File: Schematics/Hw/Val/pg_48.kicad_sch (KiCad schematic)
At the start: 20 parts, among them U5001 F30, U5002 F151, U5003 F37, U5004 F37, U5005 F04, U5006 F02, U5007 F00, U5008 F37, U5009 F37, U5010 F04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

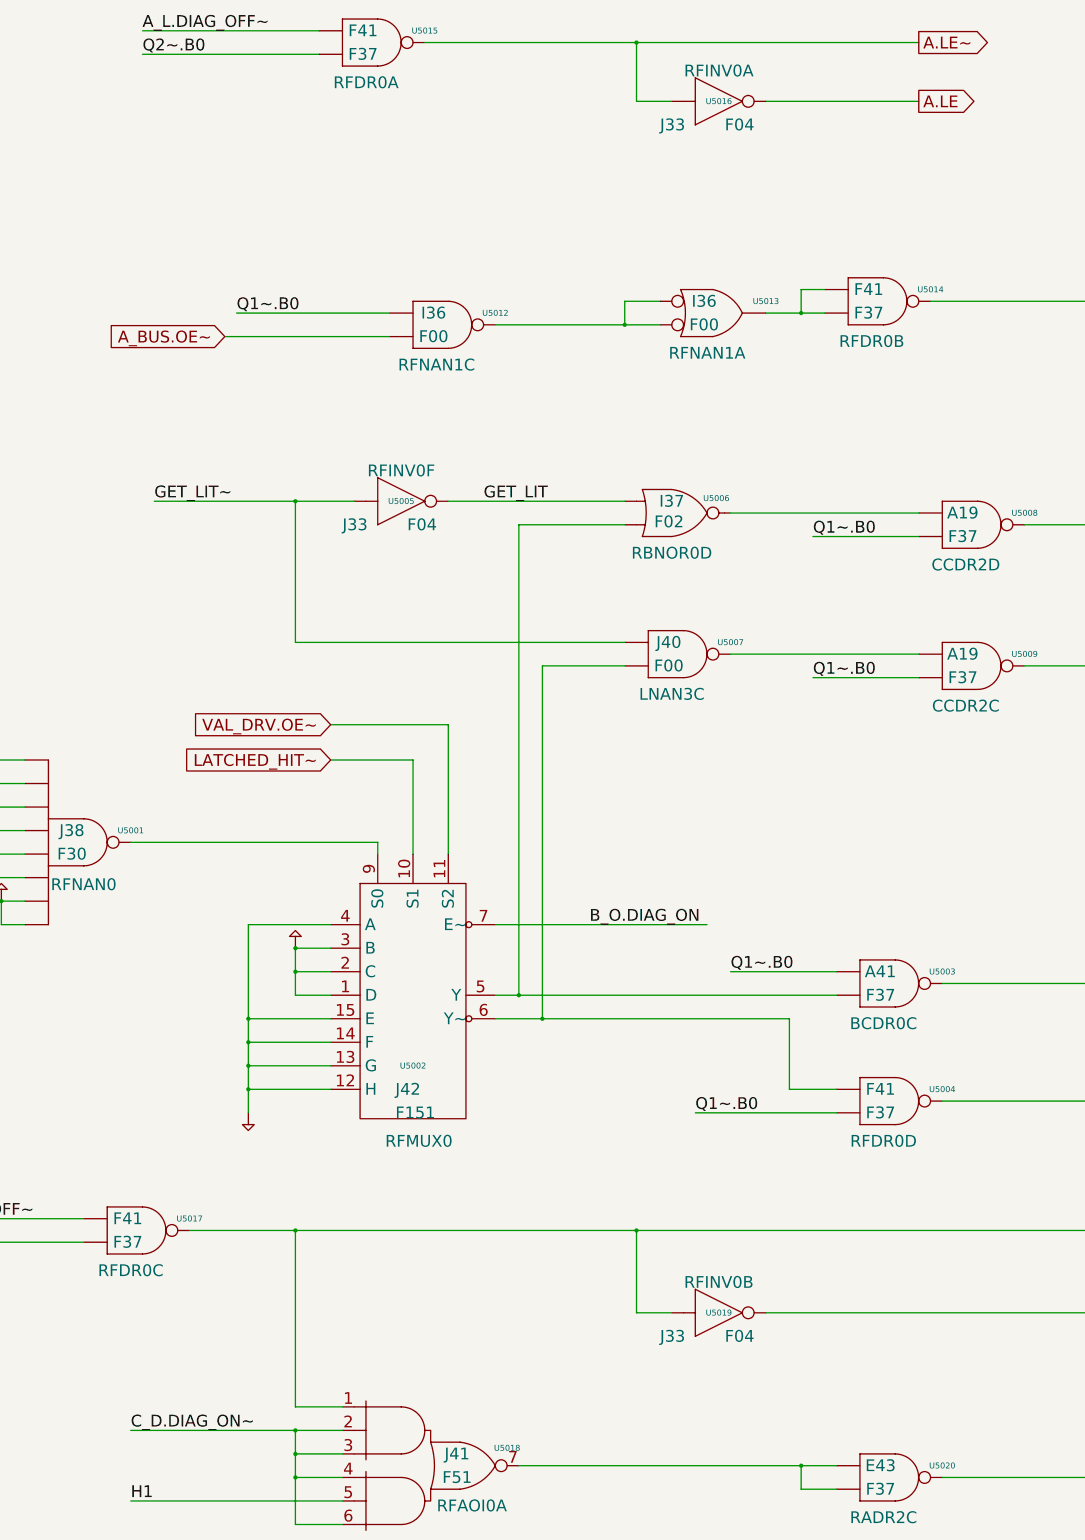
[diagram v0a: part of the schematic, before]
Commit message: Upgrade to KiCad9
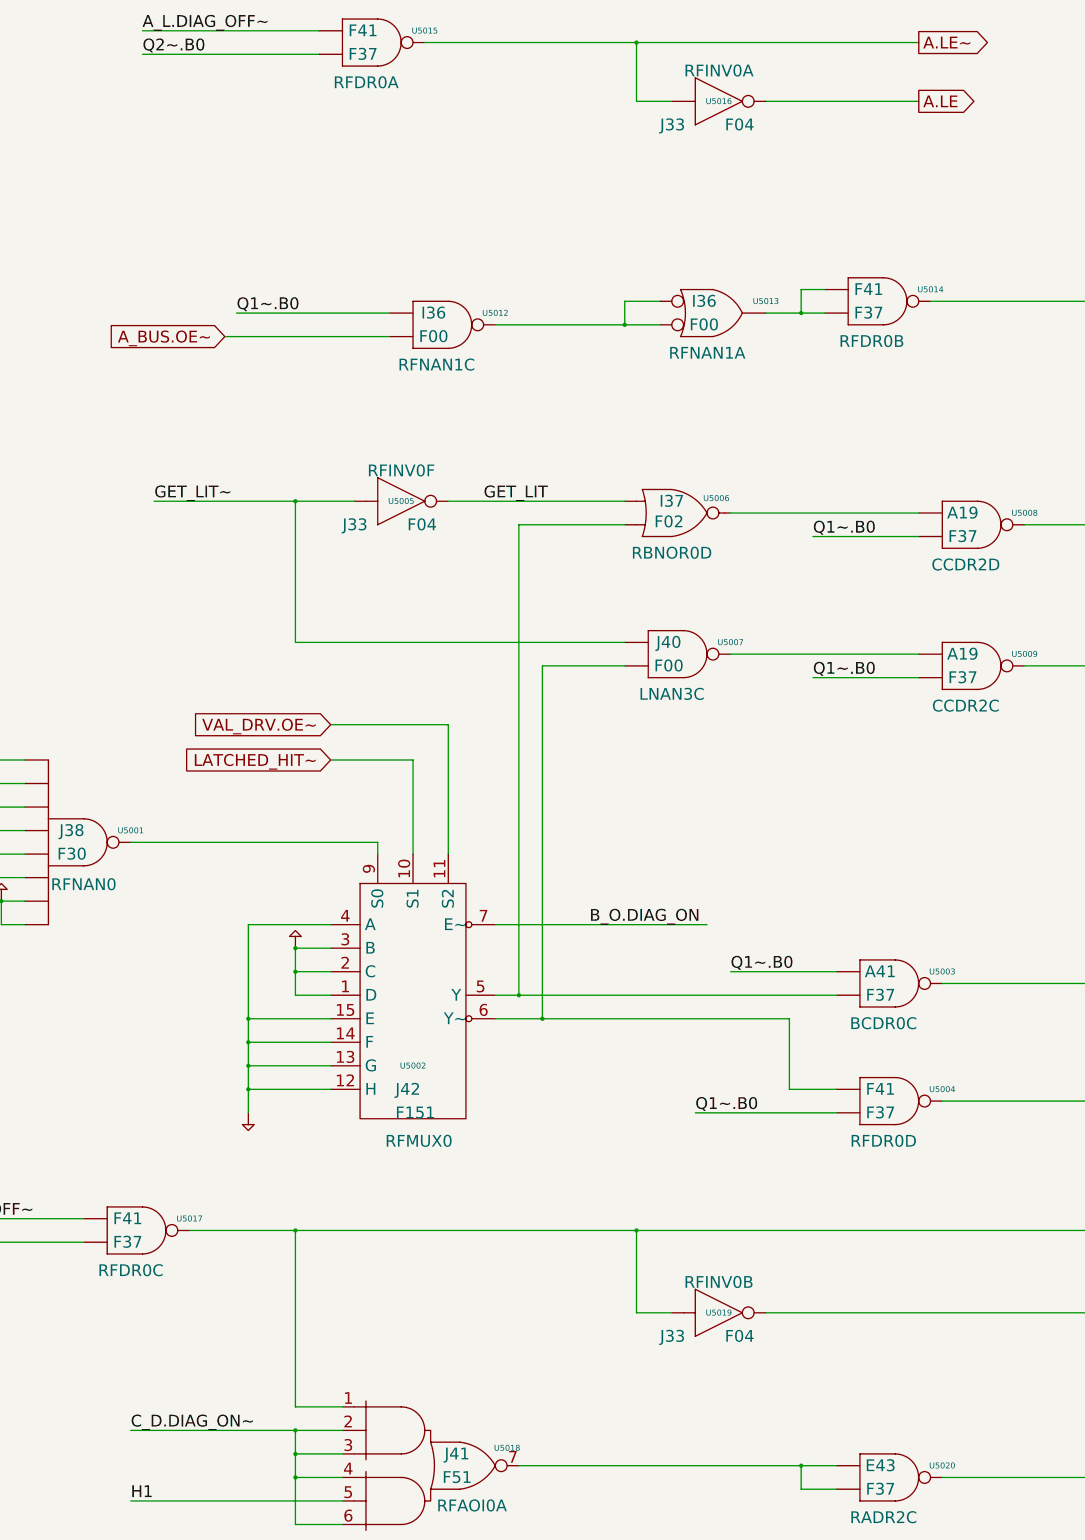
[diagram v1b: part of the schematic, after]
